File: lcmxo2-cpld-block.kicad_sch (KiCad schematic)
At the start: 40 parts, among them J12 PMOD, J13 Raspberry_Pi_2_3, SW6 BTN, SW7 BTN, SW8 BTN, U9 LCMXO2-1200HC-4TG100I

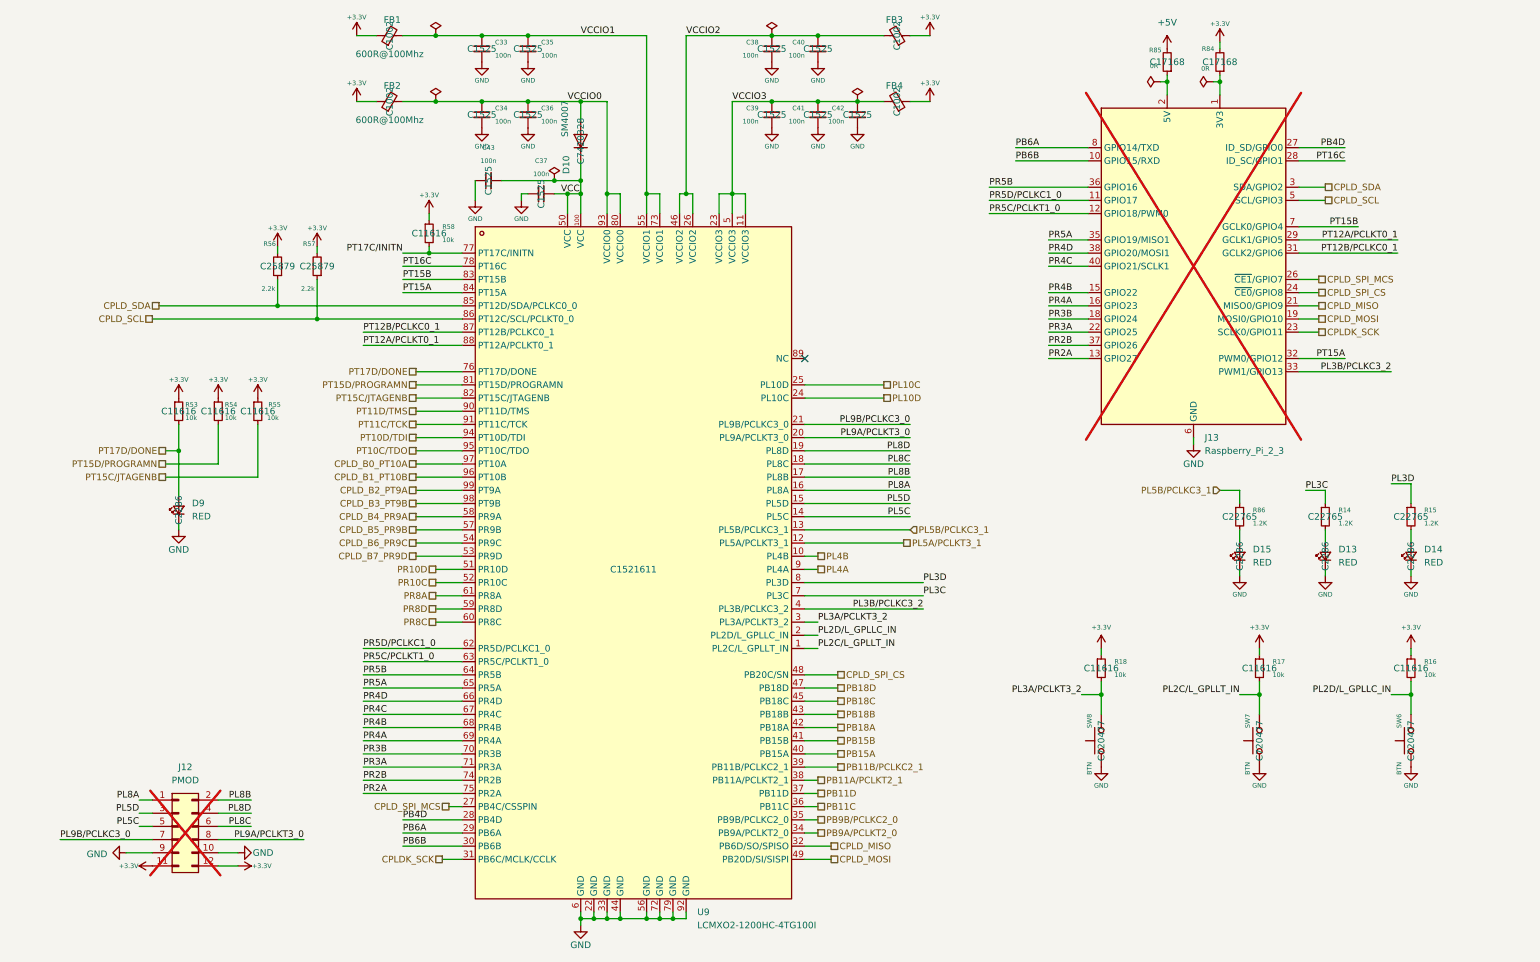
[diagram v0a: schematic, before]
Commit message: Rework on pins assignements
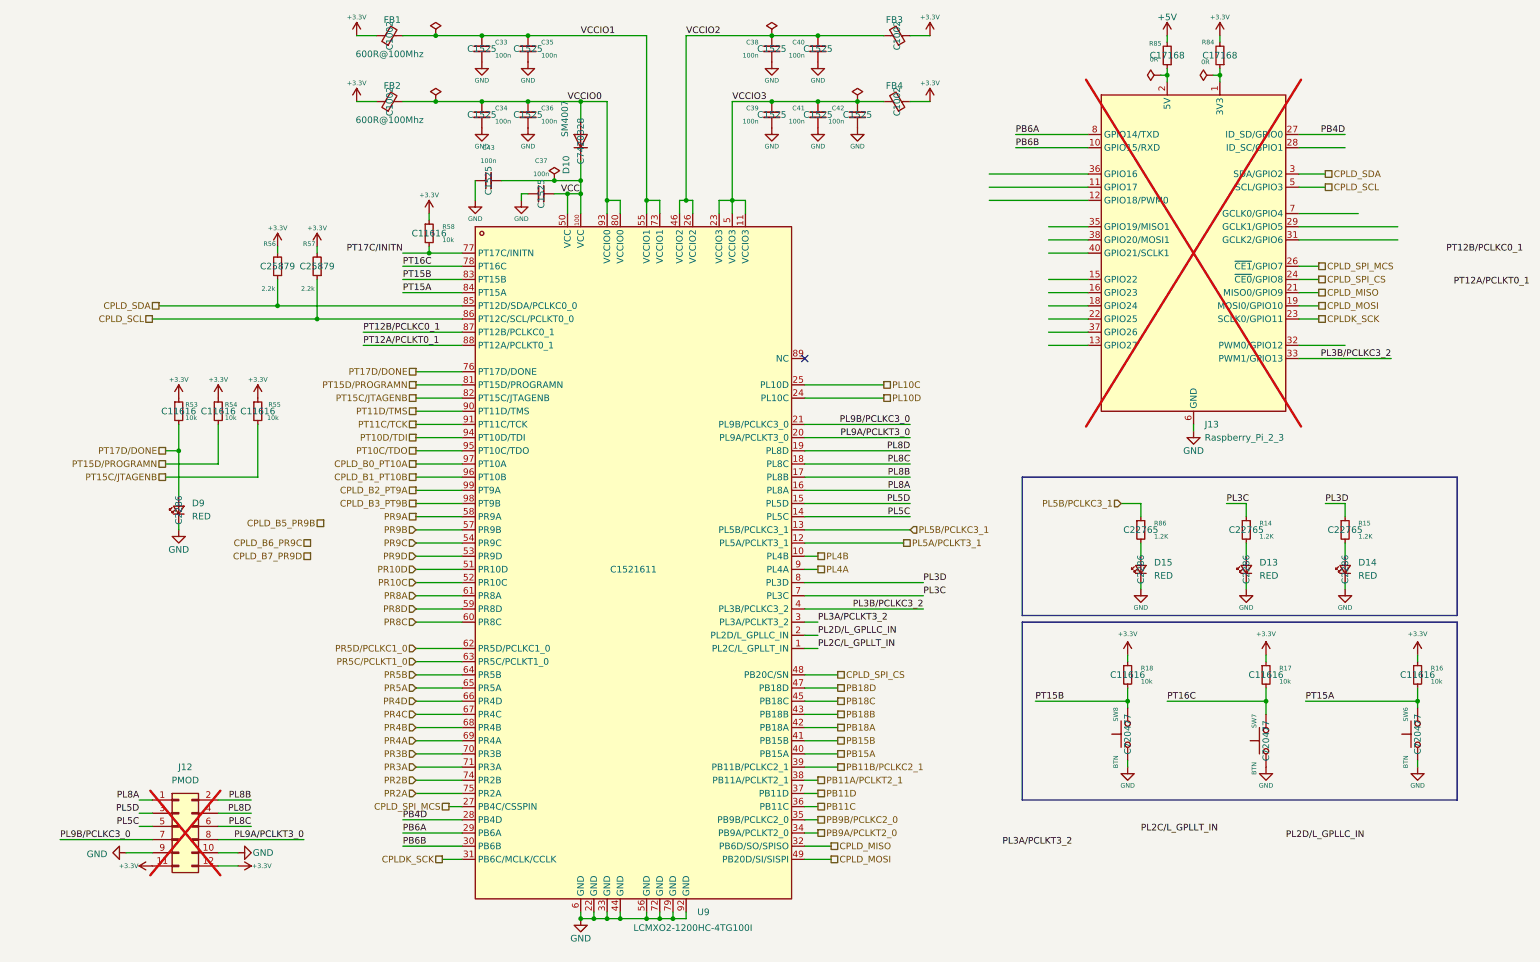
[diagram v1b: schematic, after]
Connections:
- net CPLD_B5_PR9B: no longer U9.57 (PR9B)
- net CPLD_B6_PR9C: no longer U9.54 (PR9C)
- net CPLD_B7_PR9D: no longer U9.53 (PR9D)
- net PL2C/L_GPLLT_IN: no longer R17.2, SW7.2
- net PL2D/L_GPLLC_IN: no longer R16.2, SW6.2
- net PL3A/PCLKT3_2: no longer R18.2, SW8.2
- net PR2A: no longer J13.13 (GPIO27)
- net PR2B: no longer J13.37 (GPIO26)
- net PR3A: no longer J13.22 (GPIO25)
- net PR3B: no longer J13.18 (GPIO24)
- net PR4A: no longer J13.16 (GPIO23)
- net PR4B: no longer J13.15 (GPIO22)
- net PR4C: no longer J13.40 (GPIO21/SCLK1)
- net PR4D: no longer J13.38 (GPIO20/MOSI1)
- net PR5A: no longer J13.35 (GPIO19/MISO1)
- net PR5B: no longer J13.36 (GPIO16)
- net PR5C/PCLKT1_0: no longer J13.12 (GPIO18/PWM0)
- net PR5D/PCLKC1_0: no longer J13.11 (GPIO17)
- net PT12A/PCLKT0_1: no longer J13.29 (GCLK1/GPIO5)
- net PT12B/PCLKC0_1: no longer J13.31 (GCLK2/GPIO6)
- net PT15A: now also R16.2, SW6.2; no longer J13.32 (PWM0/GPIO12)
- net PT15B: now also R18.2, SW8.2; no longer J13.7 (GCLK0/GPIO4)
- net PT16C: now also R17.2, SW7.2; no longer J13.28 (ID_SC/GPIO1)
- net CPLD_B4_PR9A renamed PR9A
- new net PR9B: U9.57 (PR9B)
- new net PR9C: U9.54 (PR9C)
- new net PR9D: U9.53 (PR9D)
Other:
- moved on the sheet: D13, D14, D15, J13, R14, R15, R16, R17, R18, R84, R85, R86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

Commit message: Rework on pins assignements
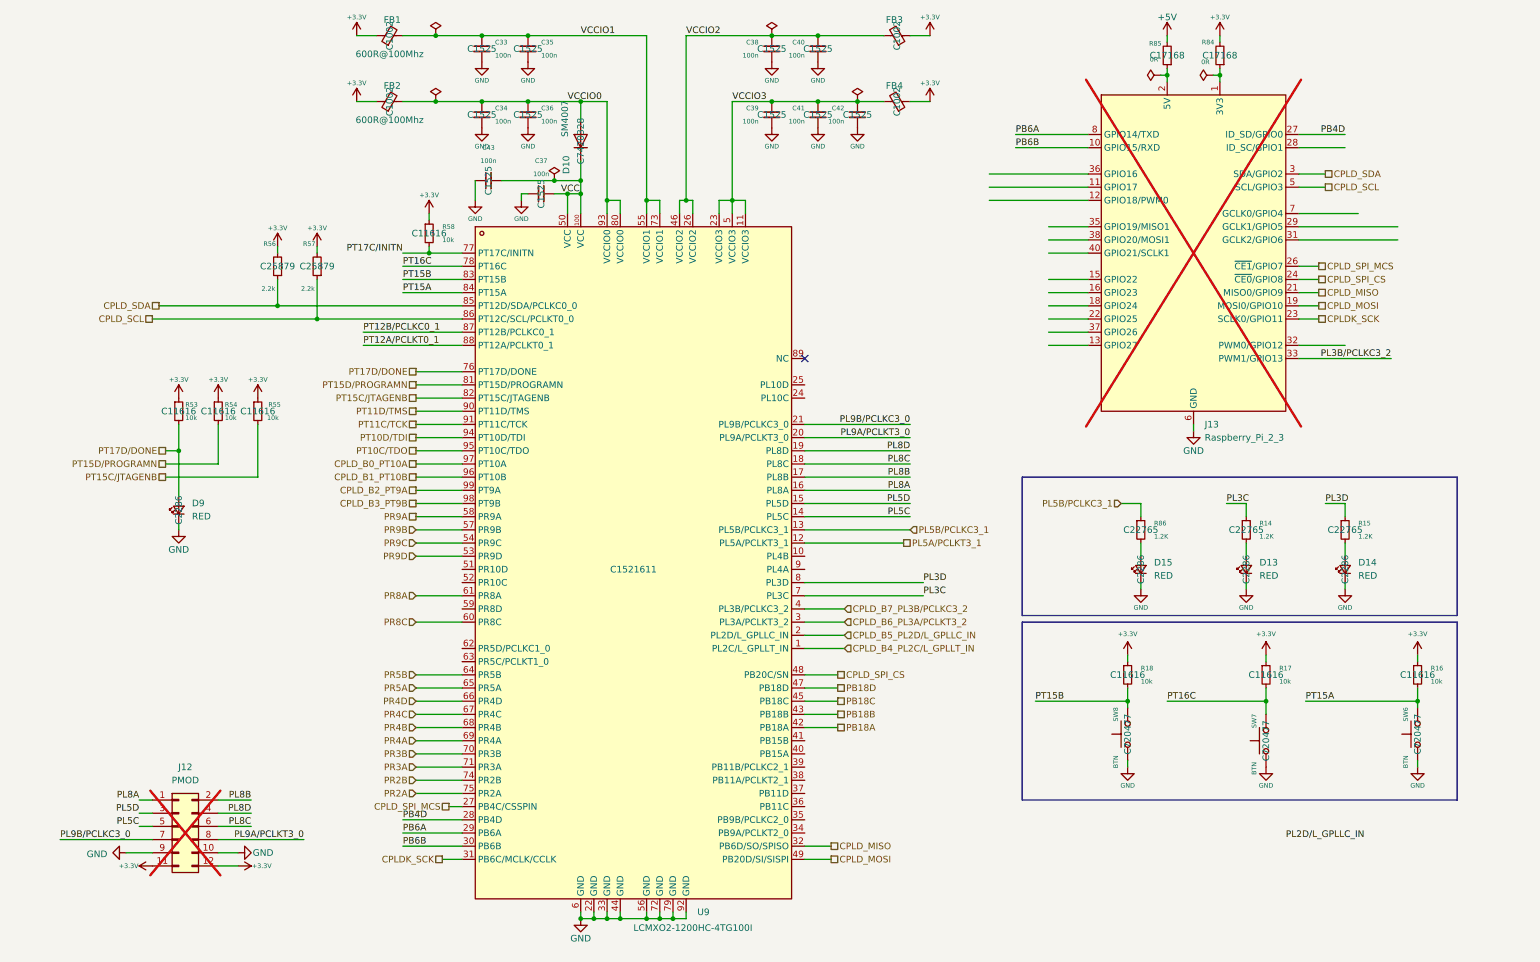
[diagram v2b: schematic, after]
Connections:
- net PL2D/L_GPLLC_IN: no longer U9.2 (PL2D/L_GPLLC_IN)
- net PL3B/PCLKC3_2: no longer U9.4 (PL3B/PCLKC3_2)
- net PB11A/PCLKT2_1: no longer names the net of U9.38 (PB11A/PCLKT2_1)
- net PB11B/PCLKC2_1: no longer names the net of U9.39 (PB11B/PCLKC2_1)
- net PB11C: no longer names the net of U9.36 (PB11C)
- net PB11D: no longer names the net of U9.37 (PB11D)
- net PB15A: no longer names the net of U9.40 (PB15A)
- net PB15B: no longer names the net of U9.41 (PB15B)
- net PB9A/PCLKT2_0: no longer names the net of U9.34 (PB9A/PCLKT2_0)
- net PB9B/PCLKC2_0: no longer names the net of U9.35 (PB9B/PCLKC2_0)
- net PL10C: no longer names the net of U9.25 (PL10D)
- net PL10D: no longer names the net of U9.24 (PL10C)
- net PL2C/L_GPLLT_IN renamed CPLD_B4_PL2C/L_GPLLT_IN
- net PL3A/PCLKT3_2 renamed CPLD_B6_PL3A/PCLKT3_2
- net PL4A: no longer names the net of U9.9 (PL4A)
- net PL4B: no longer names the net of U9.10 (PL4B)
- net PR10C: no longer names the net of U9.52 (PR10C)
- net PR10D: no longer names the net of U9.51 (PR10D)
- net PR5C/PCLKT1_0: no longer names the net of U9.63 (PR5C/PCLKT1_0)
- net PR5D/PCLKC1_0: no longer names the net of U9.62 (PR5D/PCLKC1_0)
- net PR8D: no longer names the net of U9.59 (PR8D)
- new net CPLD_B5_PL2D/L_GPLLC_IN: U9.2 (PL2D/L_GPLLC_IN)
- new net CPLD_B7_PL3B/PCLKC3_2: U9.4 (PL3B/PCLKC3_2)

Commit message: Update the source code
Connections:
- net PL3B/PCLKC3_2 is gone; now on net PB11A/PCLKT2_1: J13.33 (PWM1/GPIO13)
- net PT12A/PCLKT0_1: now also J13.38 (GPIO20/MOSI1)
- net PT12B/PCLKC0_1: now also J13.35 (GPIO19/MISO1)
- net PR10C: now reaches J13.11 (GPIO17)
- net PR10C: now also U9.52 (PR10C)
- net PL10C: now reaches J13.12 (GPIO18/PWM0)
- net PL10C: now also U9.24 (PL10C)
- net PB15A: now reaches J13.13 (GPIO27)
- net PB15A: now also U9.40 (PB15A)
- net PB11C: now reaches J13.15 (GPIO22)
- net PB11C: now also U9.36 (PB11C)
- net PB11D: now reaches J13.16 (GPIO23)
- net PB11D: now also U9.37 (PB11D)
- net PL10D: now reaches J13.18 (GPIO24)
- net PL10D: now also U9.25 (PL10D)
- net PB11B/PCLKC2_1: now reaches J13.22 (GPIO25)
- net PB11B/PCLKC2_1: now also U9.39 (PB11B/PCLKC2_1)
- net PL4A: now reaches J13.28 (ID_SC/GPIO1)
- net PL4A: now also U9.9 (PL4A)
- net PR5C/PCLKT1_0: now reaches J13.29 (GCLK1/GPIO5)
- net PR5C/PCLKT1_0: now also U9.63 (PR5C/PCLKT1_0)
- net PR5D/PCLKC1_0: now reaches J13.31 (GCLK2/GPIO6)
- net PR5D/PCLKC1_0: now also U9.62 (PR5D/PCLKC1_0)
- net PB9B/PCLKC2_0: now reaches J13.32 (PWM0/GPIO12)
- net PB9B/PCLKC2_0: now also U9.35 (PB9B/PCLKC2_0)
- net PR10D: now reaches J13.36 (GPIO16)
- net PR10D: now also U9.51 (PR10D)
- net PB15B: now reaches J13.37 (GPIO26)
- net PB15B: now also U9.41 (PB15B)
- net PB9A/PCLKT2_0: now reaches J13.40 (GPIO21/SCLK1)
- net PB9A/PCLKT2_0: now also U9.34 (PB9A/PCLKT2_0)
- net PL4B: now reaches J13.7 (GCLK0/GPIO4)
- net PL4B: now also U9.10 (PL4B)
- net PB11A/PCLKT2_1: now reaches U9.38 (PB11A/PCLKT2_1)
- net PR8D: now reaches U9.59 (PR8D)

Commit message: Update the source code
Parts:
- added J1005: JTAG JUMP, Connector_PinSocket_2.54mm:PinSocket_2x05_P2.54mm_Vertical, symbol Connector_Generic:Conn_02x05_Odd_Even
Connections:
- net PB18A: now also J1005.2 (Pin_2)
- net PB18B: now also J1005.4 (Pin_4)
- net PB18C: now also J1005.1 (Pin_1)
- net PB18D: now also J1005.3 (Pin_3)
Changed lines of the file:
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@@
 	(wire
 		(pts
+			(xy 50.8 146.05) (xy 44.45 146.05)
+		)
+		(stroke
+			(width 0)
+			(type default)
+		)
+	)
+	(wire
+		(pts
 			(xy 226.06 25.4) (xy 227.33 25.4)
 		)
@@
 	(wire
 		(pts
+			(xy 50.8 148.59) (xy 44.45 148.59)
+		)
+		(stroke
+			(width 0)
+			(type default)
+		)
+	)
+	(wire
+		(pts
 			(xy 72.39 77.47) (xy 91.44 77.47)
 		)
@@
 	(wire
 		(pts
+			(xy 27.94 146.05) (xy 31.75 146.05)
+		)
+		(stroke
+			(width 0)
+			(type default)
+		)
+	)
+	(wire
+		(pts
 			(xy 82.55 146.05) (xy 91.44 146.05)
 		)
@@
 	(wire
 		(pts
+			(xy 27.94 148.59) (xy 31.75 148.59)
+		)
+		(stroke
+			(width 0)
+			(type default)
+		)
+	)
+	(wire
+		(pts
 			(xy 163.83 143.51) (xy 157.48 143.51)
 		)
@@
 		)
 	)
+	(label "PB18A"
+		(at 27.94 148.59 180)
+		(effects
+			(font
+				(size 1.27 1.27)
+			)
+			(justify right bottom)
+		)
+	)
 	(label "PL8C"
 		(at 50.8 170.18 180)
@@
 		)
 	)
+	(label "PB18D"
+		(at 50.8 146.05 0)
+		(effects
+			(font
+				(size 1.27 1.27)
+			)
+			(justify left bottom)
+		)
+	)
 	(label "PL5D"
 		(at 177.8 107.95 180)
@@
 		)
 	)
+	(label "PB18B"
+		(at 27.94 146.05 180)
+		(effects
+			(font
+				(size 1.27 1.27)
+			)
+			(justify right bottom)
+		)
+	)
 	(label "PL5C"
 		(at 177.8 110.49 180)
@@
 		)
 	)
+	(label "PB18C"
+		(at 50.8 148.59 0)
+		(effects
+			(font
+				(size 1.27 1.27)
+			)
+			(justify left bottom)
+		)
+	)
 	(label "PL8C"
 		(at 177.8 100.33 180)
@@
 					(unit 1)
 				)
+			)
+		)
+	)
+	(symbol
+		(lib_id "Connector_Generic:Conn_02x05_Odd_Even")
+		(at 39.37 143.51 180)
+		(unit 1)
+		(exclude_from_sim no)
+		(in_bom no)
+		(on_board yes)
+		(dnp yes)
+		(property "Reference" "J1005"
+			(at 39.37 135.89 0)
+			(effects
+				(font
+					(size 1.27 1.27)
+				)
+			)
+		)
+		(property "Value" "JTAG JUMP"
+			(at 39.116 152.146 0)
+			(effects
+				(font
+					(size 1.27 1.27)
+				)
+			)
+		)
+		(property "Footprint" "Connector_PinSocket_2.54mm:PinSocket_2x05_P2.54mm_Vertical"
+			(at 39.37 120.142 0)
+			(effects
+				(font
+					(size 1.27 1.27)
+				)
+				(hide yes)
+			)
+		)
+		(property "Datasheet" "~"
+			(at 39.37 143.51 0)
+			(effects
+				(font
+					(size 1.27 1.27)
+				)
+				(hide yes)
+			)
+		)
+		(property "Description" "Generic connector, double row, 02x05, odd/even pin numbering scheme (row 1 odd numbers, row 2 even numbers), script generated (kicad-library-utils/schlib/autogen/connector/)"
+			(at 39.37 143.51 0)
+			(effects
+				(font
+					(size 1.27 1.27)
+				)
+				(hide yes)
+			)
+		)
+		(pin "6"
+		)
+		(pin "3"
+		)
+		(pin "10"
+		)
+		(pin "4"
+		)
+		(pin "7"
+		)
+		(pin "1"
+		)
+		(pin "9"
+		)
+		(pin "8"
+		)
+		(pin "5"
+		)
+		(pin "2"
+		)
+		(instances
+			(project "stm32-fpga-bootloader"
+				(path "/5ed49623-6cbc-4a61-8fb3-1814d185ddb6/78f79e27-5991-443e-9657-8ff8f155d4b1"
+					(reference "J1005")
+					(unit 1)
+				)

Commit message: Update the source files
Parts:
- added J6001: Conn_02x06_Odd_Even, Connector_PinSocket_2.54mm:PinSocket_2x06_P2.54mm_Vertical, symbol Connector_Generic:Conn_02x06_Odd_Even
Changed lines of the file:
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@@
 					(size 1.27 1.27)
 				)
+				(hide yes)
 			)
 		)
@@
 					(size 1.27 1.27)
 				)
+				(hide yes)
 			)
 		)
@@
 					(size 1.27 1.27)
 				)
+				(hide yes)
 			)
 		)
@@
 					(size 1.27 1.27)
 				)
+				(hide yes)
 			)
 		)
@@
 					(unit 1)
 				)
+			)
+		)
+	)
+	(symbol
+		(lib_id "Connector_Generic:Conn_02x06_Odd_Even")
+		(at 15.24 133.35 0)
+		(unit 1)
+		(exclude_from_sim no)
+		(in_bom yes)
+		(on_board yes)
+		(dnp no)
+		(fields_autoplaced yes)
+		(property "Reference" "J6001"
+			(at 16.51 121.92 0)
+			(effects
+				(font
+					(size 1.27 1.27)
+				)
+			)
+		)
+		(property "Value" "Conn_02x06_Odd_Even"
+			(at 16.51 124.46 0)
+			(effects
+				(font
+					(size 1.27 1.27)
+				)
+			)
+		)
+		(property "Footprint" "Connector_PinSocket_2.54mm:PinSocket_2x06_P2.54mm_Vertical"
+			(at 15.24 133.35 0)
+			(effects
+				(font
+					(size 1.27 1.27)
+				)
+				(hide yes)
+			)
+		)
+		(property "Datasheet" "~"
+			(at 15.24 133.35 0)
+			(effects
+				(font
+					(size 1.27 1.27)
+				)
+				(hide yes)
+			)
+		)
+		(property "Description" "Generic connector, double row, 02x06, odd/even pin numbering scheme (row 1 odd numbers, row 2 even numbers), script generated (kicad-library-utils/schlib/autogen/connector/)"
+			(at 15.24 133.35 0)
+			(effects
+				(font
+					(size 1.27 1.27)
+				)
+				(hide yes)
+			)
+		)
+		(pin "5"
+		)
+		(pin "7"
+		)
+		(pin "9"
+		)
+		(pin "4"
+		)
+		(pin "8"
+		)
+		(pin "1"
+		)
+		(pin "10"
+		)
+		(pin "12"
+		)
+		(pin "6"
+		)
+		(pin "2"
+		)
+		(pin "11"
+		)
+		(pin "3"
+		)
+		(instances
+			(project ""
+				(path "/5ed49623-6cbc-4a61-8fb3-1814d185ddb6/78f79e27-5991-443e-9657-8ff8f155d4b1"
+					(reference "J6001")
+					(unit 1)
+				)
